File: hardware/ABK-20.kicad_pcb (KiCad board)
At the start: 2 copper layers, 90 x 90 mm, 72 parts, among them J1 CONN_01X04, J2 CONN_01X04, J3 CONN_02X03, J4 Con_3-5V, J5 USB_C_6P, J6 Sync_Jumper, SW1 SW_SPST, SW2 SW_Push, SW3 SW_SPDT_MSM, SW4 SW_Push, U1 ATTINY85-20SU, U2 PAM8002, U3 7805

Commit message: fix(pcb, footprints): shift Bourns slide pot right side pads +2.5mm in Y to match physical part
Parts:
- J3: moved to F.Cu
- J5: moved to B.Cu
- moved J3 2.58 mm to (73.7, 71.1), turned to 90 degrees
- moved Speaker1 0.55 mm to (154.7, 86.1)
- moved J5 0.28 mm to (114.8, 30.4), turned to 0 degrees
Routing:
- net GND: track 553.7 -> 524.7 mm
- net Net-(J5-CC2): track 40.4 -> 34.4 mm, vias 2 -> 1
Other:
- board text removed: "8Bit Mixtape - ABK-20"
- board text removed: "AUDIO / SYNC"
- board text removed: "MODE"
- board text removed: "PITCH / CV"

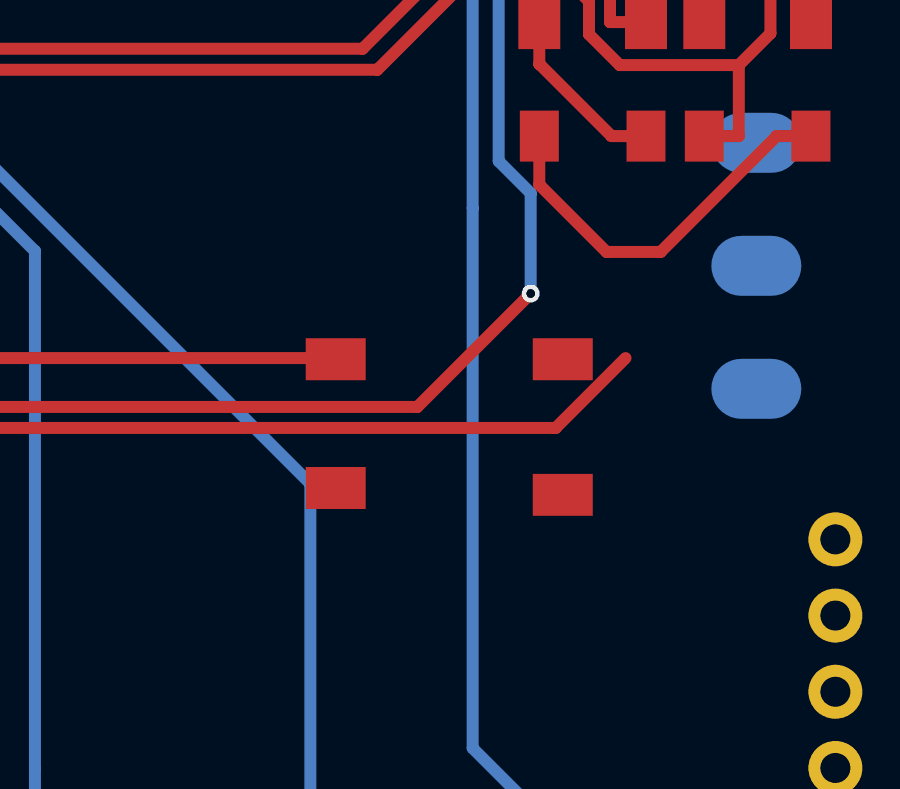
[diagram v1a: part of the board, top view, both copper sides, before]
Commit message: feat(hardware): add Highly KS01-BL-13 illuminated keypad button footprint and 3D model for SW2
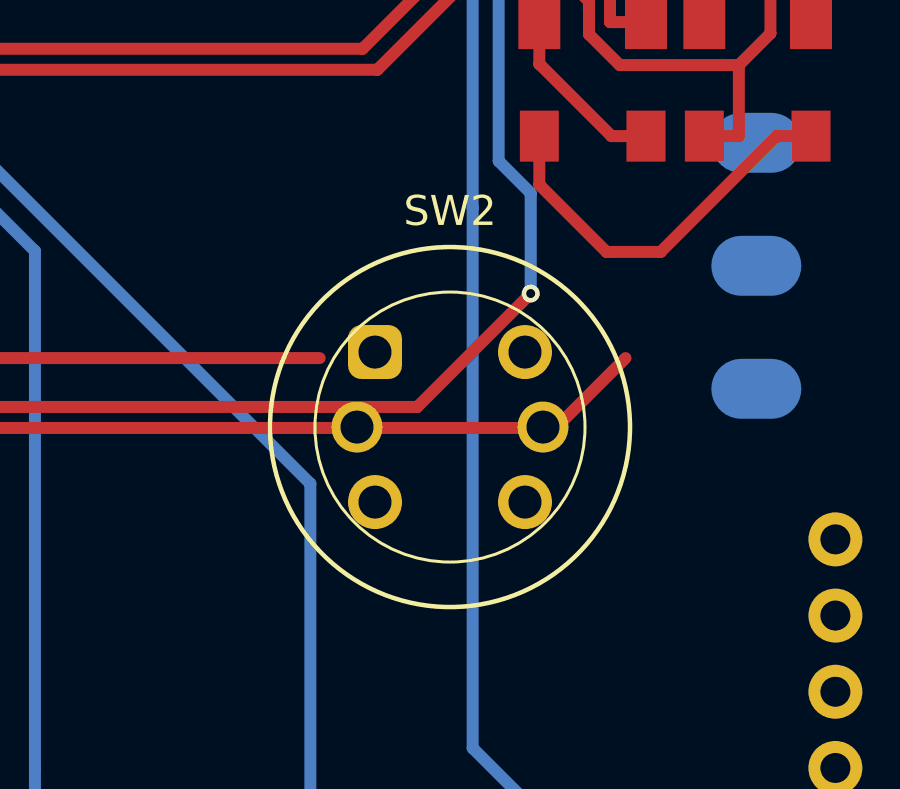
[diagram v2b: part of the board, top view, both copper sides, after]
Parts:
- SW2: footprint 8Bitmixtape_reworked:TACTILE-PTH_6mm_SMD -> 8Bitmixtape_reworked:SW_Push_Highly_KS01-BL-13
- turned SW2 to 0 degrees
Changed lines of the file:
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@@
 		)
 	)
-	(footprint "8Bitmixtape_reworked:TACTILE-PTH_6mm_SMD"
+(footprint "8Bitmixtape_reworked:SW_Push_Highly_KS01-BL-13"
 		(layer "F.Cu")
-		(at 136.9568 103.9622 180)
-		(descr "OMRON SWITCH")
-		(tags "OMRON SWITCH")
+		(at 136.9568 103.9622 0)
+		(descr "Highly Electric KS01-BL-13 Illuminated Keypad Switch, round frosted cap D=12mm, Bi-color LED, https://www.tme.eu/ch/en/details/ks01-bl-13/keypad-switches/highly-electric/ks01-blv-13/")
+		(tags "Highly KS01 KS01-BL-13 switch button illuminated LED tactile THT 12mm")
 		(property "Reference" "SW2"
-			(at 0 2.032 0)
-			(layer "Eco2.User")
-			(effects
-				(font
-					(size 1 1)
-					(thickness 0.127)
-				)
-			)
-		)
-		(property "Value" "SW_Push"
-			(at -5.842 -0.14 90)
-			(layer "Eco2.User")
+			(at 0 -7.2 0)
+			(layer "F.SilkS")
 			(effects
 				(font
@@
 			)
 		)
-		(property "Datasheet" ""
+		(property "Value" "SW_Push"
+			(at 0 7.5 0)
+			(layer "F.Fab")
+			(effects
+				(font
+					(size 1 1)
+					(thickness 0.15)
+				)
+			)
+		)
+		(property "Datasheet" "https://www.tme.eu/Document/445b24673c2c7fe28e59716d9a77095b/KS01+series.pdf"
 			(at 0 0 0)
-			(layer "B.Fab")
+			(layer "F.Fab")
 			(hide yes)
 			(effects
@@
 					(thickness 0.15)
 				)
-				(justify mirror)
 			)
 		)
-		(property "Description" ""
+		(property "Description" "Highly Electric KS01-BL-13 Illuminated Push Button"
 			(at 0 0 0)
-			(layer "B.Fab")
+			(layer "F.Fab")
 			(hide yes)
 			(effects
@@
 					(thickness 0.15)
 				)
-				(justify mirror)
 			)
 		)
 		(sheetname "/")
 		(sheetfile "ABK-20.kicad_sch")
-		(attr exclude_from_pos_files)
-		(fp_line
-			(start 3.048 0.99568)
-			(end 3.048 -1.016)
+		(attr through_hole)
+		(fp_circle
+			(center 0 0)
+			(end 6 0)
 			(stroke
-				(width 0.2032)
+				(width 0.15)
 				(type solid)
 			)
-			(layer "Eco2.User")
-		)
-		(fp_line
-			(start 2.159 3.048)
-			(end -2.159 3.048)
-			(stroke
-				(width 0.2032)
-				(type solid)
-			)
-			(layer "Eco2.User")
-		)
-		(fp_line
-			(start -2.032 1.27)
-			(end -2.032 0.508)
-			(stroke
-				(width 0.2032)
-				(type solid)
-			)
-			(layer "Eco2.User")
-		)
-		(fp_line
-			(start -2.032 0.508)
-			(end -1.651 -0.381)
-			(stroke
-				(width 0.2032)
-				(type solid)
-			)
-			(layer "Eco2.User")
-		)
-		(fp_line
-			(start -2.032 -0.508)
-			(end -2.032 -1.27)
-			(stroke
-				(width 0.2032)
-				(type solid)
-			)
-			(layer "Eco2.User")
-		)
-		(fp_line
-			(start -2.159 -3.048)
-			(end 2.159 -3.048)
-			(stroke
-				(width 0.2032)
-				(type solid)
-			)
-			(layer "Eco2.User")
-		)
-		(fp_line
-			(start -3.048 1.02616)
-			(end -3.048 -1.016)
-			(stroke
-				(width 0.2032)
-				(type solid)
-			)
-			(layer "Eco2.User")
+			(fill no)
+			(layer "F.SilkS")
 		)
 		(fp_circle
 			(center 0 0)
-			(end -0.889 -0.889)
+			(end 4.5 0)
 			(stroke
-				(width 0.1016)
+				(width 0.1)
 				(type solid)
 			)
 			(fill no)
-			(layer "Eco2.User")
+			(layer "F.SilkS")
 		)
-		(pad "1" smd rect
-			(at -3.7592 2.2606 180)
-			(size 2 1.4)
-			(layers "F.Cu" "F.Mask" "F.Paste")
+		(fp_circle
+			(center 0 0)
+			(end 6.25 0)
+			(stroke
+				(width 0.05)
+				(type solid)
+			)
+			(fill no)
+			(layer "F.CrtYd")
+		)
+		(fp_circle
+			(center 0 0)
+			(end 6 0)
+			(stroke
+				(width 0.1)
+				(type solid)
+			)
+			(fill no)
+			(layer "F.Fab")
+		)
+		(fp_circle
+			(center 0 0)
+			(end 4.5 0)
+			(stroke
+				(width 0.1)
+				(type solid)
+			)
+			(fill no)
+			(layer "F.Fab")
+		)
+		(pad "1" thru_hole roundrect
+			(at -2.5 -2.5)
+			(size 1.8 1.8)
+			(drill 1.1)
+			(layers "*.Cu" "*.Mask")
+			(roundrect_rratio 0.25)
+			(remove_unused_layers no)
 			(net 65 "Net-(R16-Pad2)")
 			(pinfunction "1")
 			(pintype "passive")
-			(solder_mask_margin 0.01)
 		)
-		(pad "1" smd rect
-			(at 3.81 2.2606 180)
-			(size 2 1.4)
-			(layers "F.Cu" "F.Mask" "F.Paste")
+		(pad "1" thru_hole circle
+			(at 2.5 -2.5)
+			(size 1.8 1.8)
+			(drill 1.1)
+			(layers "*.Cu" "*.Mask")
+			(remove_unused_layers no)
 			(net 65 "Net-(R16-Pad2)")
 			(pinfunction "1")
 			(pintype "passive")
-			(solder_mask_margin 0.01)
 		)
-		(pad "2" smd rect
-			(at -3.7592 -2.2606 180)
-			(size 2 1.4)
-			(layers "F.Cu" "F.Mask" "F.Paste")
+		(pad "2" thru_hole circle
+			(at -2.5 2.5)
+			(size 1.8 1.8)
+			(drill 1.1)
+			(layers "*.Cu" "*.Mask")
+			(remove_unused_layers no)
 			(net 3 "GND")
 			(pinfunction "2")
 			(pintype "passive")
-			(solder_mask_margin 0.01)
 		)
-		(pad "2" smd rect
-			(at 3.81 -2.032 180)
-			(size 2 1.4)
-			(layers "F.Cu" "F.Mask" "F.Paste")
+		(pad "2" thru_hole circle
+			(at 2.5 2.5)
+			(size 1.8 1.8)
+			(drill 1.1)
+			(layers "*.Cu" "*.Mask")
+			(remove_unused_layers no)
 			(net 3 "GND")
 			(pinfunction "2")
 			(pintype "passive")
-			(solder_mask_margin 0.01)
+		)
+		(pad "A" thru_hole circle
+			(at -3.1 0)
+			(size 1.7 1.7)
+			(drill 1.1)
+			(layers "*.Cu" "*.Mask")
+			(remove_unused_layers no)
+		)
+		(pad "K" thru_hole circle
+			(at 3.1 0)
+			(size 1.7 1.7)
+			(drill 1.1)
+			(layers "*.Cu" "*.Mask")
+			(remove_unused_layers no)
 		)
 		(embedded_fonts no)
-		(model "${KICAD9_3DMODEL_DIR}/Button_Switch_SMD.3dshapes/SW_SPST_Omron_B3FS-100xP.step"
+		(model "${KIPRJMOD}/3d_models/SW_Push_Highly_KS01-BL-13.wrl"
 			(offset
 				(xyz 0 0 0)

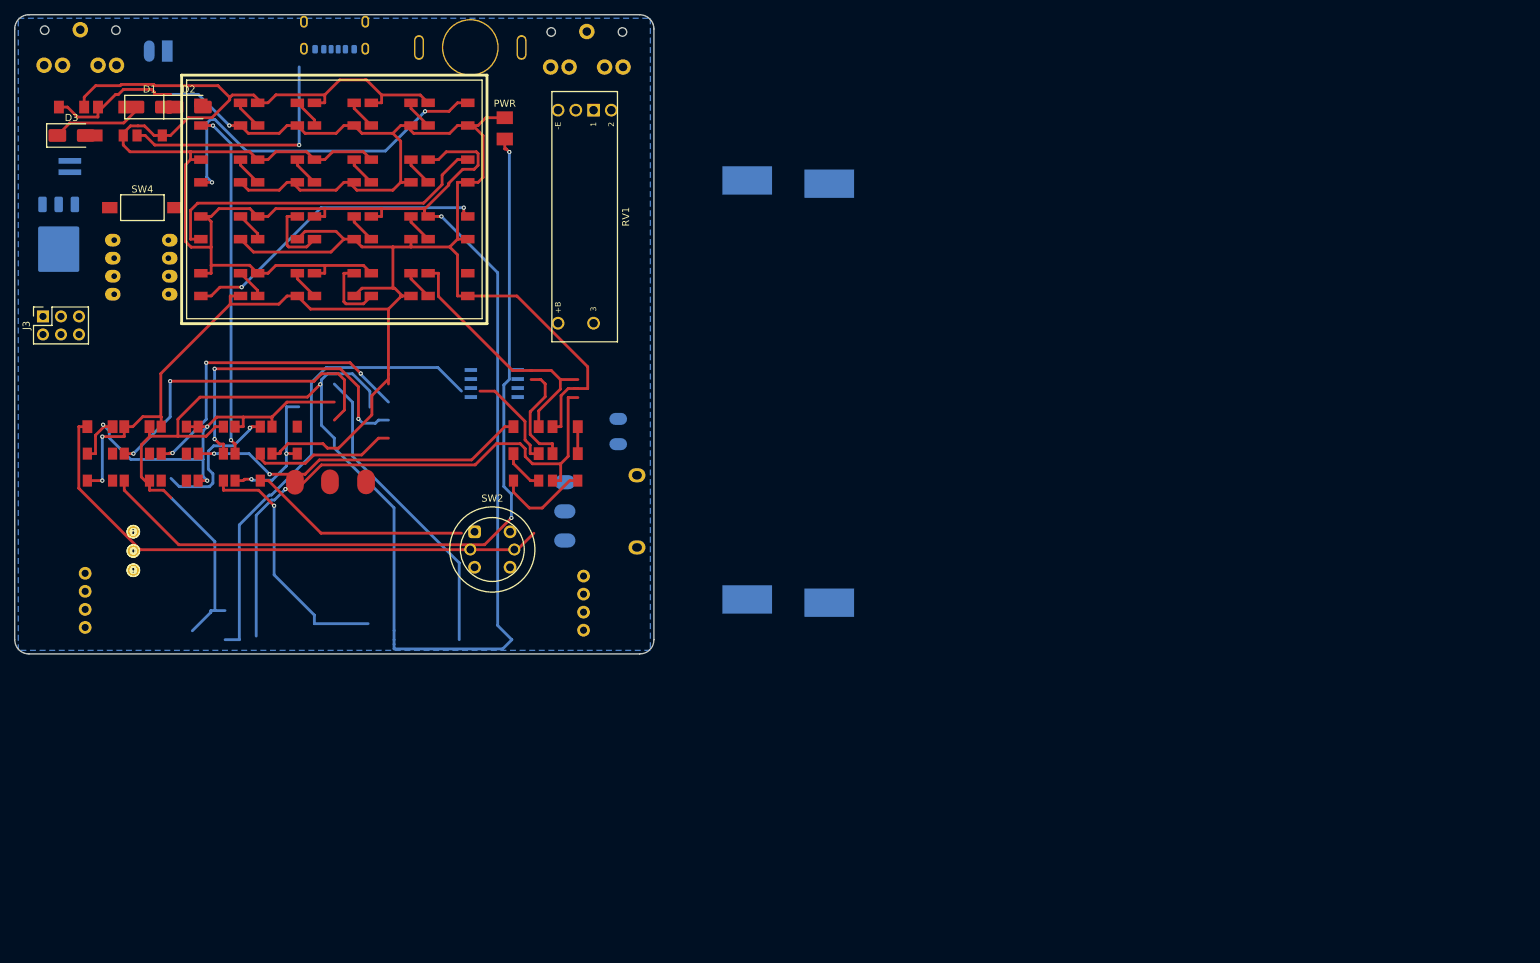
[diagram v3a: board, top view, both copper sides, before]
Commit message: refactor(pcb): reset pcb layout, clear all tracks/vias/zones and arrange footprints outside board
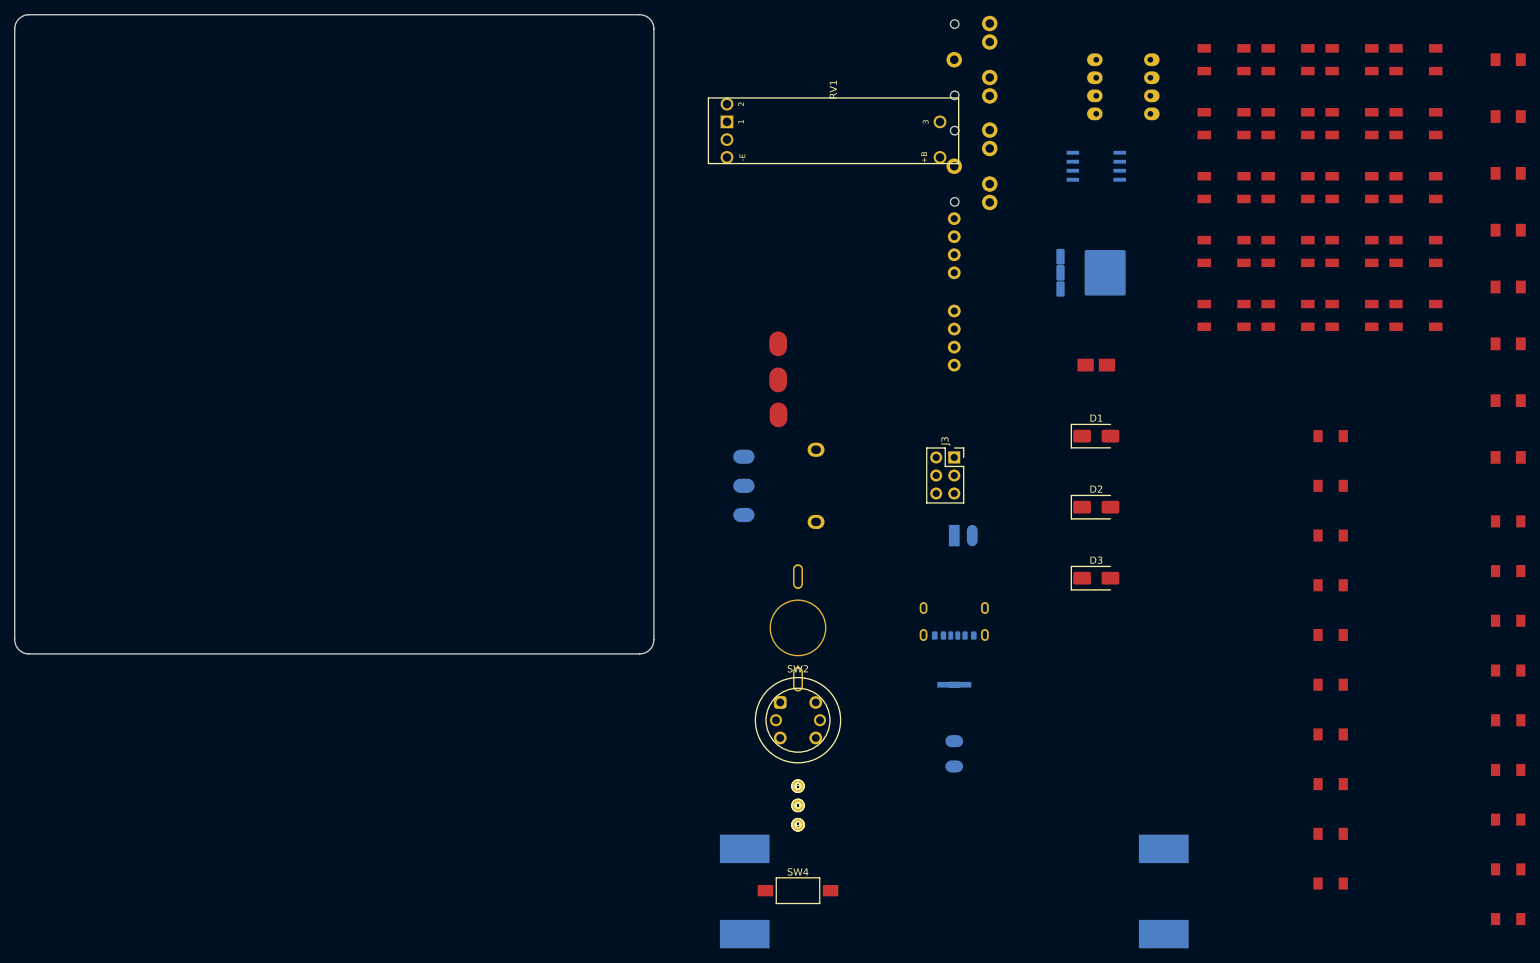
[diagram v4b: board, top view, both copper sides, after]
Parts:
- moved C7 206.5 mm to (280.0, 83.0)
- moved C1 204.9 mm to (280.0, 35.0)
- moved C8 202.9 mm to (280.0, 91.0)
- moved R5 201.8 mm to (280.0, 128.0)
- moved R6 198.2 mm to (280.0, 135.0)
- moved C2 198.0 mm to (280.0, 43.0)
- moved R7 194.8 mm to (280.0, 142.0)
- moved R17 194.6 mm to (255.0, 137.0)
- moved R18 193.2 mm to (255.0, 144.0)
- moved R8 191.8 mm to (280.0, 149.0)
- moved R9 189.2 mm to (280.0, 156.0)
- moved R1 188.4 mm to (280.0, 100.0)
- moved R2 183.8 mm to (280.0, 107.0)
- moved R3 179.6 mm to (280.0, 114.0)
- moved R4 175.7 mm to (280.0, 121.0)
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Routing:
- net GND: track 524.7 -> 0.00 mm, vias 2 -> 0
- net VCC: track 331.2 -> 0.00 mm, vias 3 -> 0
- net Net-(D-POW1-K): track 115.1 -> 0.00 mm, vias 2 -> 0
- net Net-(U2-OUT-): track 80.5 -> 0.00 mm, vias 1 -> 0
- net AudioProg: track 78.5 -> 0.00 mm
- net Net-(Jack2-T): track 66.0 -> 0.00 mm
- net PB3: track 59.1 -> 0.00 mm, vias 3 -> 0
- net Net-(NEO5-DOUT): track 51.8 -> 0.00 mm, vias 2 -> 0
- net Net-(NEO1-DIN): track 49.2 -> 0.00 mm, vias 2 -> 0
- net CV_OUT: track 48.4 -> 0.00 mm, vias 2 -> 0
- net Net-(NEO10-DOUT): track 48.3 -> 0.00 mm
- net PB4/A2: track 45.2 -> 0.00 mm, vias 2 -> 0
- net PB2/A1: track 44.3 -> 0.00 mm, vias 3 -> 0
- net Net-(NEO15-DOUT): track 43.6 -> 0.00 mm, vias 2 -> 0
- net PB1: track 43.3 -> 0.00 mm, vias 3 -> 0
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- removed copper zone on B.Cu, net GND
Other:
- board text removed: "PWR"

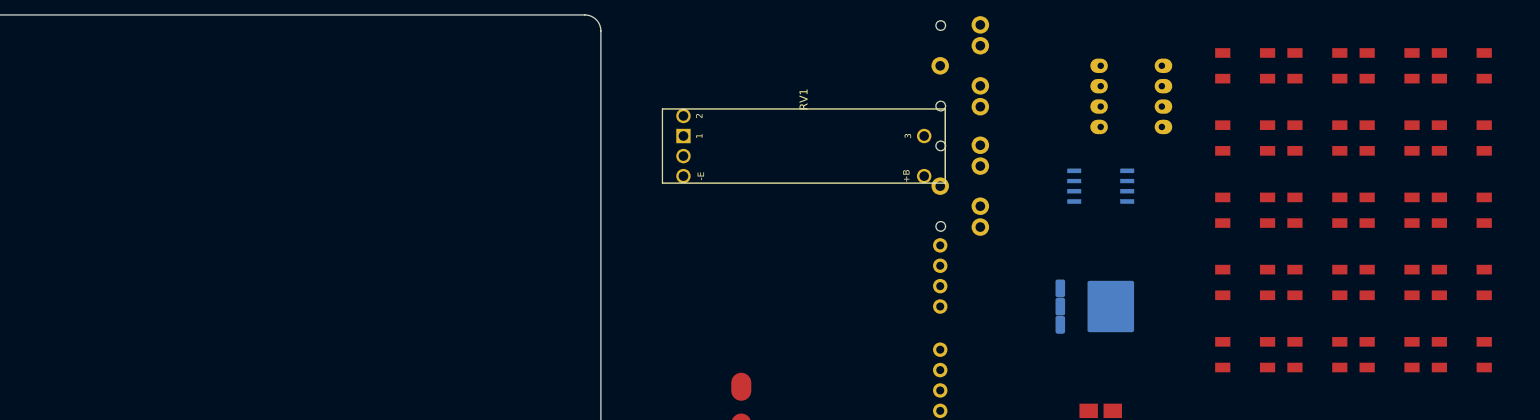
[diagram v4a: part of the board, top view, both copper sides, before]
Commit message: feat(pcb): place 5x4 NeoPixel array with BlinkeShit pitch and single-sided F.Cu snake tracks
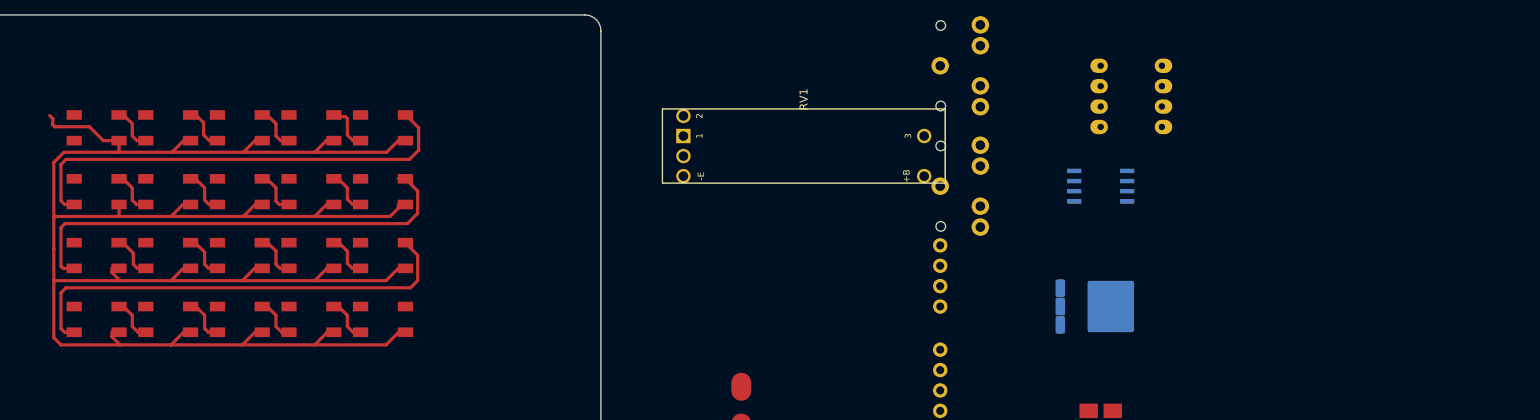
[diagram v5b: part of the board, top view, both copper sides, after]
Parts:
- moved NEO16 173.0 mm to (96.9, 66.6)
- moved NEO11 162.9 mm to (96.9, 58.6)
- moved NEO17 162.8 mm to (105.8, 66.6)
- moved NEO6 152.9 mm to (96.9, 50.7)
- moved NEO12 152.9 mm to (105.8, 58.6)
- moved NEO18 152.9 mm to (114.7, 66.6)
- moved NEO19 143.4 mm to (123.6, 66.6)
- moved NEO13 143.4 mm to (114.7, 58.6)
- moved NEO7 143.4 mm to (105.8, 50.7)
- moved NEO1 143.3 mm to (96.9, 42.7)
- moved NEO20 134.5 mm to (132.6, 66.6)
- moved NEO14 134.4 mm to (123.6, 58.6)
- moved NEO8 134.3 mm to (114.7, 50.7)
- moved NEO2 134.2 mm to (105.8, 42.7)
- moved NEO15 126.1 mm to (132.6, 58.6)
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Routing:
- net VCC: track 0.00 -> 239.5 mm
- net Net-(NEO5-DOUT): track 0.00 -> 56.7 mm
- net Net-(NEO10-DOUT): track 0.00 -> 56.7 mm
- net Net-(NEO15-DOUT): track 0.00 -> 55.9 mm
- net Net-(NEO8-DOUT): track 0.00 -> 4.16 mm
- net Net-(NEO6-DOUT): track 0.00 -> 4.15 mm
- net Net-(NEO11-DOUT): track 0.00 -> 4.11 mm
- net Net-(NEO1-DOUT): track 0.00 -> 4.10 mm
- net Net-(NEO12-DOUT): track 0.00 -> 4.10 mm
- net Net-(NEO17-DOUT): track 0.00 -> 4.08 mm
- net Net-(NEO4-DOUT): track 0.00 -> 4.08 mm
- net Net-(NEO13-DOUT): track 0.00 -> 4.07 mm
- net Net-(NEO7-DOUT): track 0.00 -> 4.05 mm
- net Net-(NEO3-DOUT): track 0.00 -> 4.04 mm
- net Net-(NEO10-DIN): track 0.00 -> 4.04 mm
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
